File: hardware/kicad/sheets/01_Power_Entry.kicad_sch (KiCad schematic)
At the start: 35 parts, among them Q101 60 V N-FET, ≤20 mΩ (TBD exact), Q102 2N7002, 60 V, U101 TPS26630PWPR (provisional), U102 TPS259470LRPW (provisional)

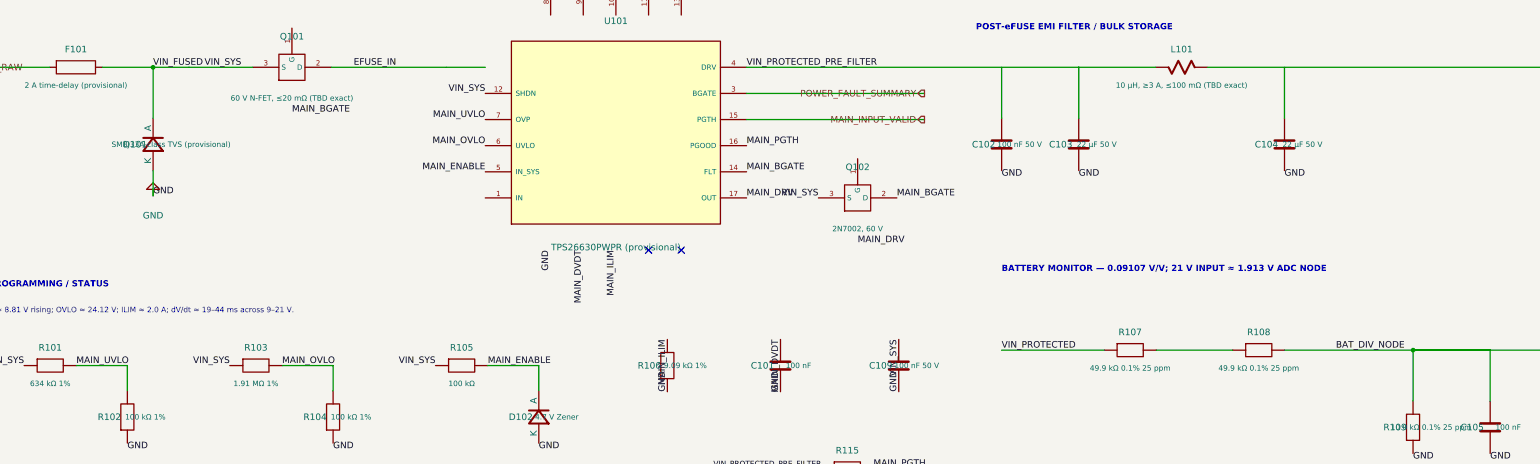
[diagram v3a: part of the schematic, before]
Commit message: Complete ECO-006 power compatibility remediation
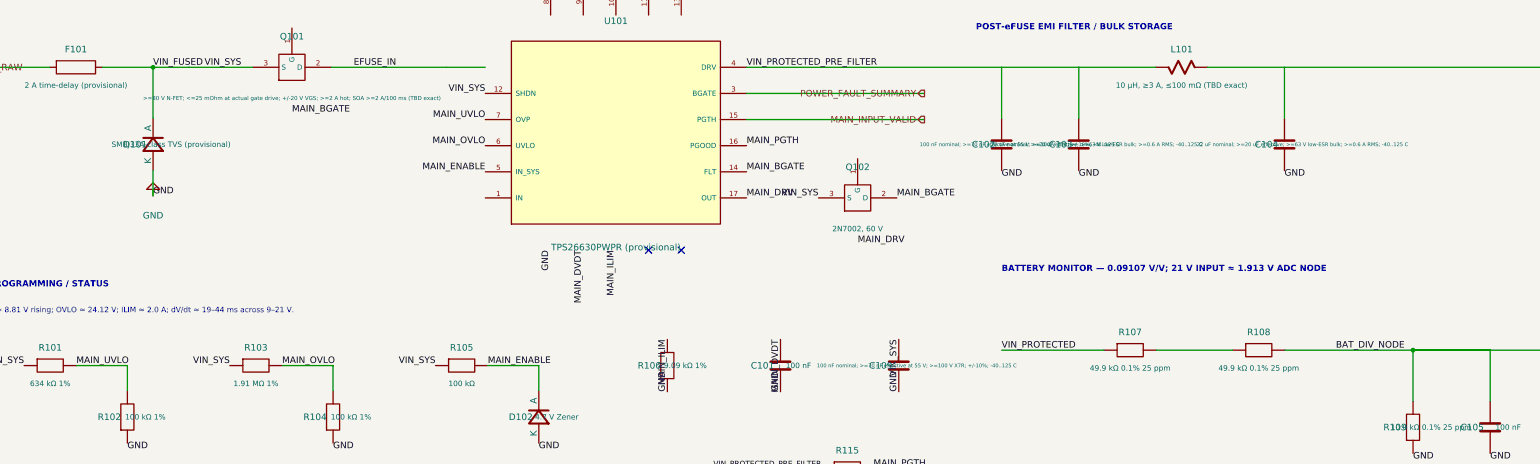
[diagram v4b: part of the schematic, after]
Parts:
- C102, C109: value 100 nF 50 V -> 100 nF nominal; >=70 nF effective at 55 V; >=100 V X7R; +/-10%; -40..125 C
- C103, C104: value 22 µF 50 V -> 22 uF nominal; >=20 uF effective; >=63 V low-ESR bulk; >=0.6 A RMS; -40..125 C
- Q101: value 60 V N-FET, ≤20 mΩ (TBD exact) -> >=80 V N-FET; <=25 mOhm at actual gate drive; +/-20 V VGS; >=2 A hot; SOA >=2 A/100 ms (TBD exact)
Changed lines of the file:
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@@
   (symbol (lib_id "IPC100:NMOS") (at 82 45 0) (unit 1) (exclude_from_sim no) (in_bom yes) (on_board yes) (dnp no)
     (property "Reference" "Q101" (at 82 39 0) (effects (font (size 1.27 1.27))))
-    (property "Value" "60 V N-FET, ≤20 mΩ (TBD exact)" (at 82 51 0) (effects (font (size 1.05 1.05))))
+    (property "Value" ">=80 V N-FET; <=25 mOhm at actual gate drive; +/-20 V VGS; >=2 A hot; SOA >=2 A/100 ms (TBD exact)" (at 82 51 0) (effects (font (size 0.78 0.78))))
     (property "Footprint" "" (at 82 45 0) (effects (font (size 1.27 1.27)) hide))
     (property "Datasheet" "" (at 82 45 0) (effects (font (size 1.27 1.27)) hide))
@@
   (symbol (lib_id "IPC100:C") (at 200 103 90) (unit 1) (exclude_from_sim no) (in_bom yes) (on_board yes) (dnp no)
  (property "Reference" "C109" (at 196.5 103 90) (effects (font (size 1.27 1.27))))
-    (property "Value" "100 nF 50 V" (at 203.5 103 90) (effects (font (size 1.05 1.05)))) (property "Footprint" "" (at 200 103 0) (effects (font (size 1 1)) hide)) (property "Datasheet" "" (at 200 103 0) (effects (font (size 1 1)) hide))
+    (property "Value" "100 nF nominal; >=70 nF effective at 55 V; >=100 V X7R; +/-10%; -40..125 C" (at 203.5 103 90) (effects (font (size 0.72 0.72)))) (property "Footprint" "" (at 200 103 0) (effects (font (size 1 1)) hide)) (property "Datasheet" "" (at 200 103 0) (effects (font (size 1 1)) hide))
     (pin "1") (pin "2")
     (instances (project "IPC-100" (path "/10000000-0000-4000-8000-000000000001/10000000-0000-4000-8000-000000000005" (reference "C109") (unit 1)))))
@@
   (symbol (lib_id "IPC100:C") (at 220 60 90) (unit 1) (exclude_from_sim no) (in_bom yes) (on_board yes) (dnp no)
  (property "Reference" "C102" (at 216.5 60 90) (effects (font (size 1.27 1.27))))
-    (property "Value" "100 nF 50 V" (at 223.5 60 90) (effects (font (size 1.05 1.05)))) (property "Footprint" "" (at 220 60 0) (effects (font (size 1 1)) hide)) (property "Datasheet" "" (at 220 60 0) (effects (font (size 1 1)) hide))
+    (property "Value" "100 nF nominal; >=70 nF effective at 55 V; >=100 V X7R; +/-10%; -40..125 C" (at 223.5 60 90) (effects (font (size 0.72 0.72)))) (property "Footprint" "" (at 220 60 0) (effects (font (size 1 1)) hide)) (property "Datasheet" "" (at 220 60 0) (effects (font (size 1 1)) hide))
     (pin "1") (pin "2")
     (instances (project "IPC-100" (path "/10000000-0000-4000-8000-000000000001/10000000-0000-4000-8000-000000000005" (reference "C102") (unit 1)))))
@@
   (symbol (lib_id "IPC100:C") (at 235 60 90) (unit 1) (exclude_from_sim no) (in_bom yes) (on_board yes) (dnp no)
  (property "Reference" "C103" (at 231.5 60 90) (effects (font (size 1.27 1.27))))
-    (property "Value" "22 µF 50 V" (at 238.5 60 90) (effects (font (size 1.05 1.05)))) (property "Footprint" "" (at 235 60 0) (effects (font (size 1 1)) hide)) (property "Datasheet" "" (at 235 60 0) (effects (font (size 1 1)) hide))
+    (property "Value" "22 uF nominal; >=20 uF effective; >=63 V low-ESR bulk; >=0.6 A RMS; -40..125 C" (at 238.5 60 90) (effects (font (size 0.72 0.72)))) (property "Footprint" "" (at 235 60 0) (effects (font (size 1 1)) hide)) (property "Datasheet" "" (at 235 60 0) (effects (font (size 1 1)) hide))
     (pin "1") (pin "2")
     (instances (project "IPC-100" (path "/10000000-0000-4000-8000-000000000001/10000000-0000-4000-8000-000000000005" (reference "C103") (unit 1)))))
@@
   (symbol (lib_id "IPC100:C") (at 275 60 90) (unit 1) (exclude_from_sim no) (in_bom yes) (on_board yes) (dnp no)
  (property "Reference" "C104" (at 271.5 60 90) (effects (font (size 1.27 1.27))))
-    (property "Value" "22 µF 50 V" (at 278.5 60 90) (effects (font (size 1.05 1.05)))) (property "Footprint" "" (at 275 60 0) (effects (font (size 1 1)) hide)) (property "Datasheet" "" (at 275 60 0) (effects (font (size 1 1)) hide))
+    (property "Value" "22 uF nominal; >=20 uF effective; >=63 V low-ESR bulk; >=0.6 A RMS; -40..125 C" (at 278.5 60 90) (effects (font (size 0.72 0.72)))) (property "Footprint" "" (at 275 60 0) (effects (font (size 1 1)) hide)) (property "Datasheet" "" (at 275 60 0) (effects (font (size 1 1)) hide))
     (pin "1") (pin "2")
     (instances (project "IPC-100" (path "/10000000-0000-4000-8000-000000000001/10000000-0000-4000-8000-000000000005" (reference "C104") (unit 1)))))

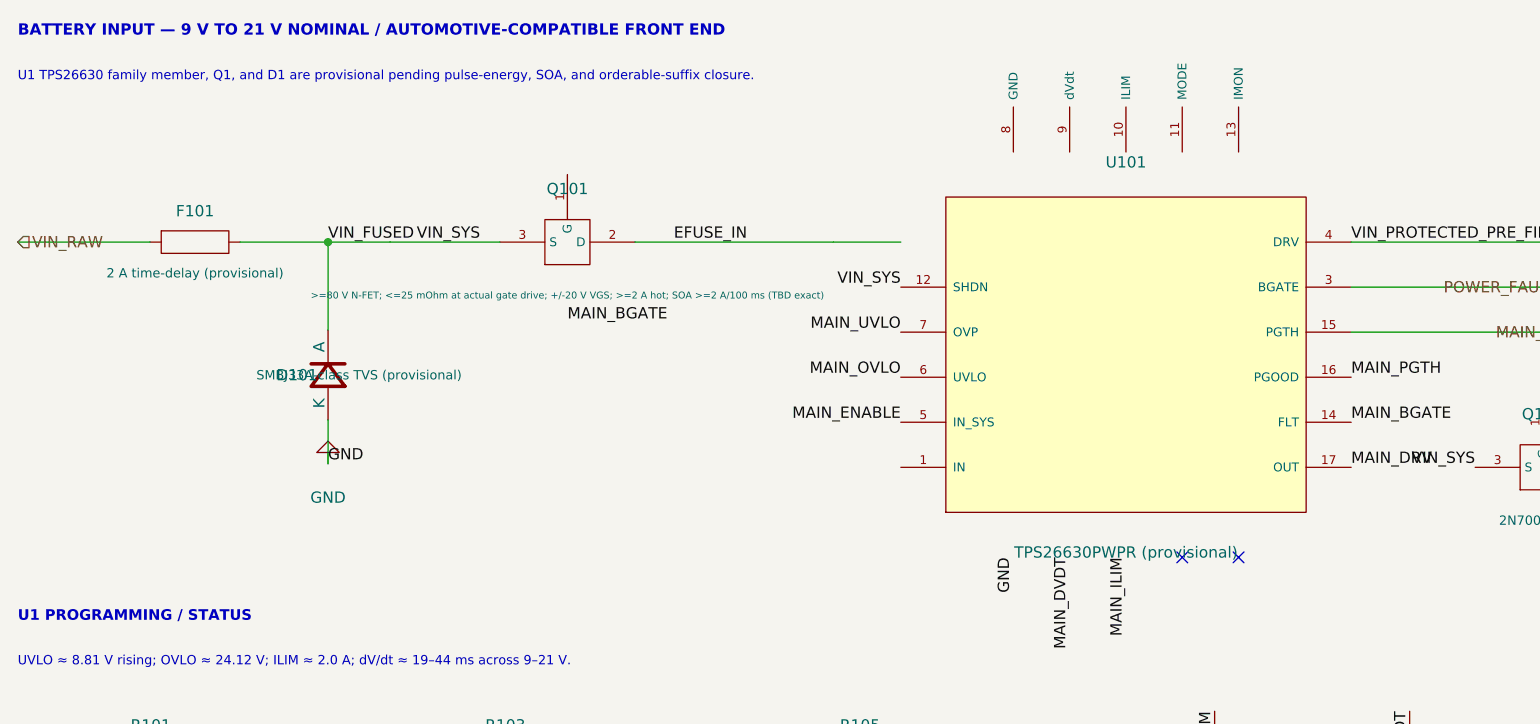
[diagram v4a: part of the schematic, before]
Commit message: Remediate power active device compatibility
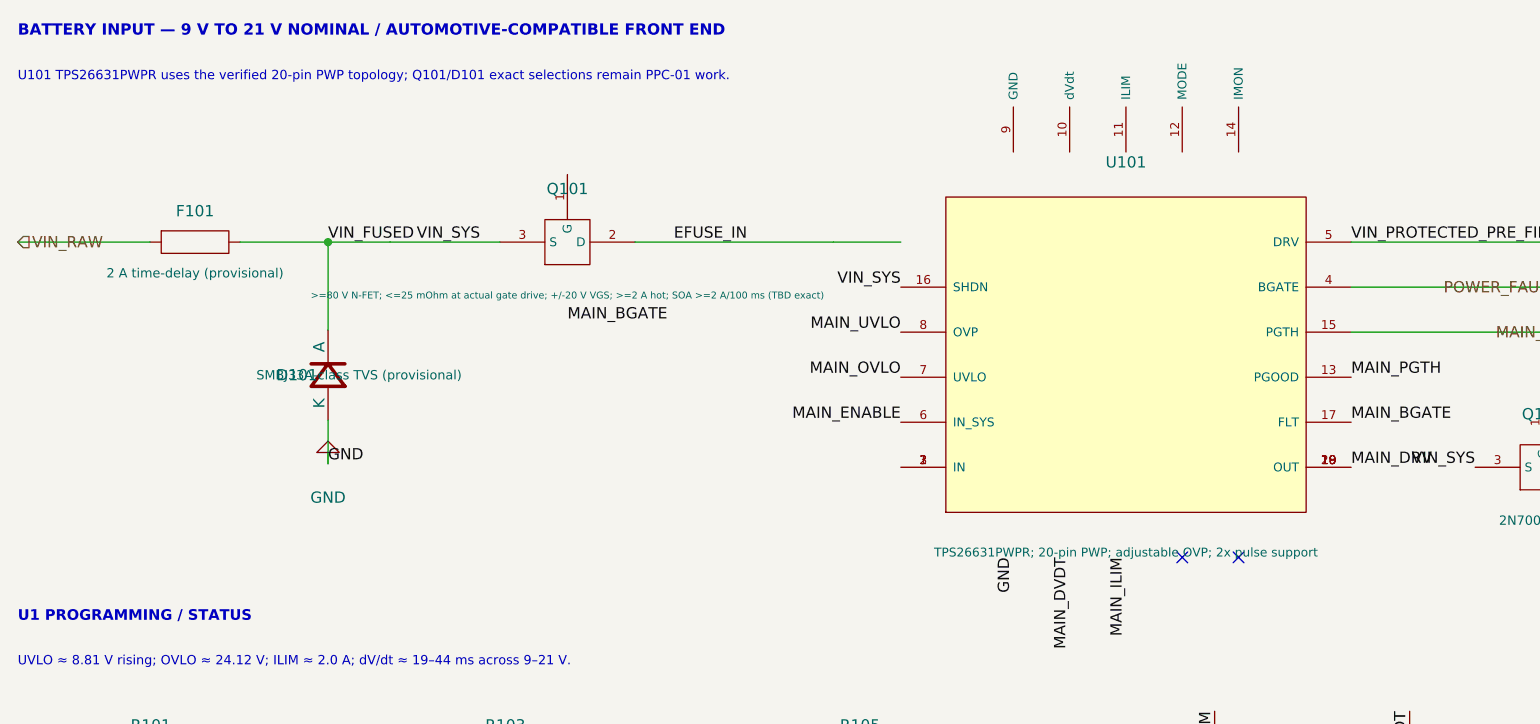
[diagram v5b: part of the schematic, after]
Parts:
- U101: value TPS26630PWPR (provisional) -> TPS26631PWPR; 20-pin PWP; adjustable OVP; 2x pulse support; symbol IPC100:TPS26630 -> IPC100:TPS26631_PWP
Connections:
- net MAIN_BGATE: now also U101.17 (FLT); no longer U101.14 (FLT)
- net MAIN_DRV: now also U101.18 (OUT), U101.19 (OUT), U101.20 (OUT); no longer U101.17 (OUT)
- net MAIN_ENABLE: now also U101.6 (IN_SYS); no longer U101.5 (IN_SYS)
- net MAIN_OVLO: now also U101.7 (UVLO); no longer U101.6 (UVLO)
- net MAIN_PGTH: now also U101.13 (PGOOD); no longer U101.16 (PGOOD)
- net MAIN_UVLO: now also U101.8 (OVP); no longer U101.7 (OVP)
- net POWER_FAULT_SUMMARY: now also U101.4 (BGATE); no longer U101.3 (BGATE)
- net VIN_FUSED: now also U101.16 (SHDN); no longer U101.12 (SHDN)
- net VIN_PROTECTED_PRE_FILTER: now also U101.5 (DRV); no longer U101.4 (DRV)
- net at U101.1 (IN): now also U101.2 (IN), U101.3 (IN)
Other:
- note added: "U101 TPS26631PWPR uses the verified 20-pin PWP topology; Q101/D101 exact selections remain PPC-01 work."
- note removed: "U1 TPS26630 family member, Q1, and D1 are provisional pending pulse-energy, SOA, and orderable-suffix closure."
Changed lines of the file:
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@@
   (text "BATTERY INPUT — 9 V TO 21 V NOMINAL / AUTOMOTIVE-COMPATIBLE FRONT END" (at 20 22 0)
     (effects (font (size 1.27 1.27) (bold yes)) (justify left bottom)))
-  (text "U1 TPS26630 family member, Q1, and D1 are provisional pending pulse-energy, SOA, and orderable-suffix closure." (at 20 27 0)
+  (text "U101 TPS26631PWPR uses the verified 20-pin PWP topology; Q101/D101 exact selections remain PPC-01 work." (at 20 27 0)
     (effects (font (size 1.05 1.05)) (justify left bottom)))
   (text "POWER_FAULT_SUMMARY is U1 FLT: open-drain, active low; pull-up and qualification belong on Sheet 06." (at 220 27 0)
@@
   (label "EFUSE_IN" (at 94 45 0) (effects (font (size 1.27 1.27)) (justify left bottom)))
   (label "MAIN_BGATE" (at 82 52.62 0) (effects (font (size 1.27 1.27)) (justify left top)))
-  (symbol (lib_id "IPC100:TPS26630") (at 145 57.7 0) (unit 1) (exclude_from_sim no) (in_bom yes) (on_board yes) (dnp no)
+  (symbol (lib_id "IPC100:TPS26631_PWP") (at 145 57.7 0) (unit 1) (exclude_from_sim no) (in_bom yes) (on_board yes) (dnp no)
     (property "Reference" "U101" (at 145 36 0) (effects (font (size 1.27 1.27))))
-    (property "Value" "TPS26630PWPR (provisional)" (at 145 80 0) (effects (font (size 1.27 1.27))))
+    (property "Value" "TPS26631PWPR; 20-pin PWP; adjustable OVP; 2x pulse support" (at 145 80 0) (effects (font (size 1 1))))
     (property "Footprint" "" (at 145 57.7 0) (effects (font (size 1.27 1.27)) hide))
     (property "Datasheet" "https://www.ti.com/lit/ds/symlink/tps2663.pdf" (at 145 57.7 0) (effects (font (size 1.27 1.27)) hide))
-    (pin "1") (pin "3")
-    (pin "4") (pin "5")
-    (pin "6") (pin "7")
-    (pin "8") (pin "9")
-    (pin "10") (pin "11")
-    (pin "12") (pin "13")
-    (pin "14") (pin "15")
-    (pin "16") (pin "17")
+    (pin "1") (pin "2") (pin "3")
+    (pin "4") (pin "5") (pin "6")
+    (pin "7") (pin "8") (pin "9")
+    (pin "10") (pin "11") (pin "12")
+    (pin "13") (pin "14") (pin "15")
+    (pin "16") (pin "17") (pin "18")
+    (pin "19") (pin "20")
     (instances (project "IPC-100" (path "/10000000-0000-4000-8000-000000000001/10000000-0000-4000-8000-000000000005" (reference "U101") (unit 1))))
   )
